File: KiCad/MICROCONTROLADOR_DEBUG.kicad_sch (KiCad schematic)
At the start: 9 parts, among them U7 PIC24HJ128GP504-I_PT, Y1 8MHz

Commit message: Errors solucionats
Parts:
- renumbered U7 to U1
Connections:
- net VDD_3V3 renamed +3.3V
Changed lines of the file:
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@@
-		)
-	)
-	(hierarchical_label "VDD_3V3"
-		(shape input)
-		(at 50.8 27.94 180)
-		(effects
-			(font
-				(size 1.27 1.27)
-			)
-			(justify right)
 		)
 	)
@@
 		(on_board yes)
 		(dnp no)
-		(property "Reference" "#FLG01"
+		(property "Reference" "#FLG02"
 			(at 78.74 48.895 0)
 			(effects
@@
 			(project ""
 				(path "/347831db-5db9-4aff-ad32-e56fd770e219/1f039355-d395-4709-b940-eff82ebe0f62"
-					(reference "#FLG01")
+					(reference "#FLG02")
 					(unit 1)
 				)
@@
 		(dnp no)
 		(fields_autoplaced yes)
-		(property "Reference" "U7"
+		(property "Reference" "U1"
 			(at 152.4 30.48 0)
 			(effects
@@
 			(project ""
 				(path "/347831db-5db9-4aff-ad32-e56fd770e219/1f039355-d395-4709-b940-eff82ebe0f62"
-					(reference "U7")
+					(reference "U1")
 					(unit 1)
 				)
@@
 		(dnp no)
 		(fields_autoplaced yes)
-		(property "Reference" "#PWR048"
+		(property "Reference" "#PWR09"
 			(at 68.58 59.69 0)
 			(effects
@@
 			(project "PROJECTE_EINES"
 				(path "/347831db-5db9-4aff-ad32-e56fd770e219/1f039355-d395-4709-b940-eff82ebe0f62"
-					(reference "#PWR048")
+					(reference "#PWR09")
 					(unit 1)
 				)
@@
 		(dnp no)
 		(fields_autoplaced yes)
-		(property "Reference" "#PWR09"
+		(property "Reference" "#PWR06"
 			(at 44.45 91.44 0)
 			(effects
@@
 			(project "PROJECTE_EINES"
 				(path "/347831db-5db9-4aff-ad32-e56fd770e219/1f039355-d395-4709-b940-eff82ebe0f62"
-					(reference "#PWR09")
+					(reference "#PWR06")
 					(unit 1)
 				)
@@
 		(dnp no)
 		(fields_autoplaced yes)
-		(property "Reference" "#PWR010"
+		(property "Reference" "#PWR07"
 			(at 60.96 91.44 0)
 			(effects
@@
 			(project "PROJECTE_EINES"
 				(path "/347831db-5db9-4aff-ad32-e56fd770e219/1f039355-d395-4709-b940-eff82ebe0f62"
-					(reference "#PWR010")
+					(reference "#PWR07")
+					(unit 1)
+				)
+			)
+		)
+	)
+	(symbol
+		(lib_id "power:+3.3V")
+		(at 50.8 27.94 0)
+		(unit 1)
+		(exclude_from_sim no)
+		(in_bom yes)
+		(on_board yes)
+		(dnp no)
+		(fields_autoplaced yes)
+		(property "Reference" "#PWR048"
+			(at 50.8 31.75 0)
+			(effects
+				(font
+					(size 1.27 1.27)
+				)
+				(hide yes)
+			)
+		)
+		(property "Value" "+3.3V"
+			(at 50.8 22.86 0)
+			(effects
+				(font
+					(size 1.27 1.27)
+				)
+			)
+		)
+		(property "Footprint" ""
+			(at 50.8 27.94 0)
+			(effects
+				(font
+					(size 1.27 1.27)
+				)
+				(hide yes)
+			)
+		)
+		(property "Datasheet" ""
+			(at 50.8 27.94 0)
+			(effects
+				(font
+					(size 1.27 1.27)
+				)
+				(hide yes)
+			)
+		)
+		(property "Description" "Power symbol creates a global label with name \"+3.3V\""
+			(at 50.8 27.94 0)
+			(effects
+				(font
+					(size 1.27 1.27)
+				)
+				(hide yes)
+			)
+		)
+		(pin "1"
+		)
+		(instances
+			(project ""
+				(path "/347831db-5db9-4aff-ad32-e56fd770e219/1f039355-d395-4709-b940-eff82ebe0f62"
+					(reference "#PWR048")
 					(unit 1)
 				)
@@
 		(dnp no)
 		(fields_autoplaced yes)
-		(property "Reference" "#PWR047"
+		(property "Reference" "#PWR08"
 			(at 67.31 44.45 0)
 			(effects
@@
 			(project "PROJECTE_EINES"
 				(path "/347831db-5db9-4aff-ad32-e56fd770e219/1f039355-d395-4709-b940-eff82ebe0f62"
-					(reference "#PWR047")
+					(reference "#PWR08")
 					(unit 1)
 				)
@@
 		(dnp no)
 		(fields_autoplaced yes)
-		(property "Reference" "#PWR045"
+		(property "Reference" "#PWR011"
 			(at 86.36 137.16 0)
 			(effects
@@
 			(project ""
 				(path "/347831db-5db9-4aff-ad32-e56fd770e219/1f039355-d395-4709-b940-eff82ebe0f62"
-					(reference "#PWR045")
+					(reference "#PWR011")
 					(unit 1)
 				)
@@
 		(dnp no)
 		(fields_autoplaced yes)
-		(property "Reference" "#PWR046"
+		(property "Reference" "#PWR010"
 			(at 78.74 58.42 0)
 			(effects
@@
 			(project "PROJECTE_EINES"
 				(path "/347831db-5db9-4aff-ad32-e56fd770e219/1f039355-d395-4709-b940-eff82ebe0f62"
-					(reference "#PWR046")
+					(reference "#PWR010")
 					(unit 1)
 				)
@@
 		(on_board yes)
 		(dnp no)
-		(property "Reference" "#FLG02"
+		(property "Reference" "#FLG03"
 			(at 93.98 48.895 0)
 			(effects
@@
 			(project "PROJECTE_EINES"
 				(path "/347831db-5db9-4aff-ad32-e56fd770e219/1f039355-d395-4709-b940-eff82ebe0f62"
-					(reference "#FLG02")
-					(unit 1)
-				)
+					(reference "#FLG03")
+					(unit 1)
+				)

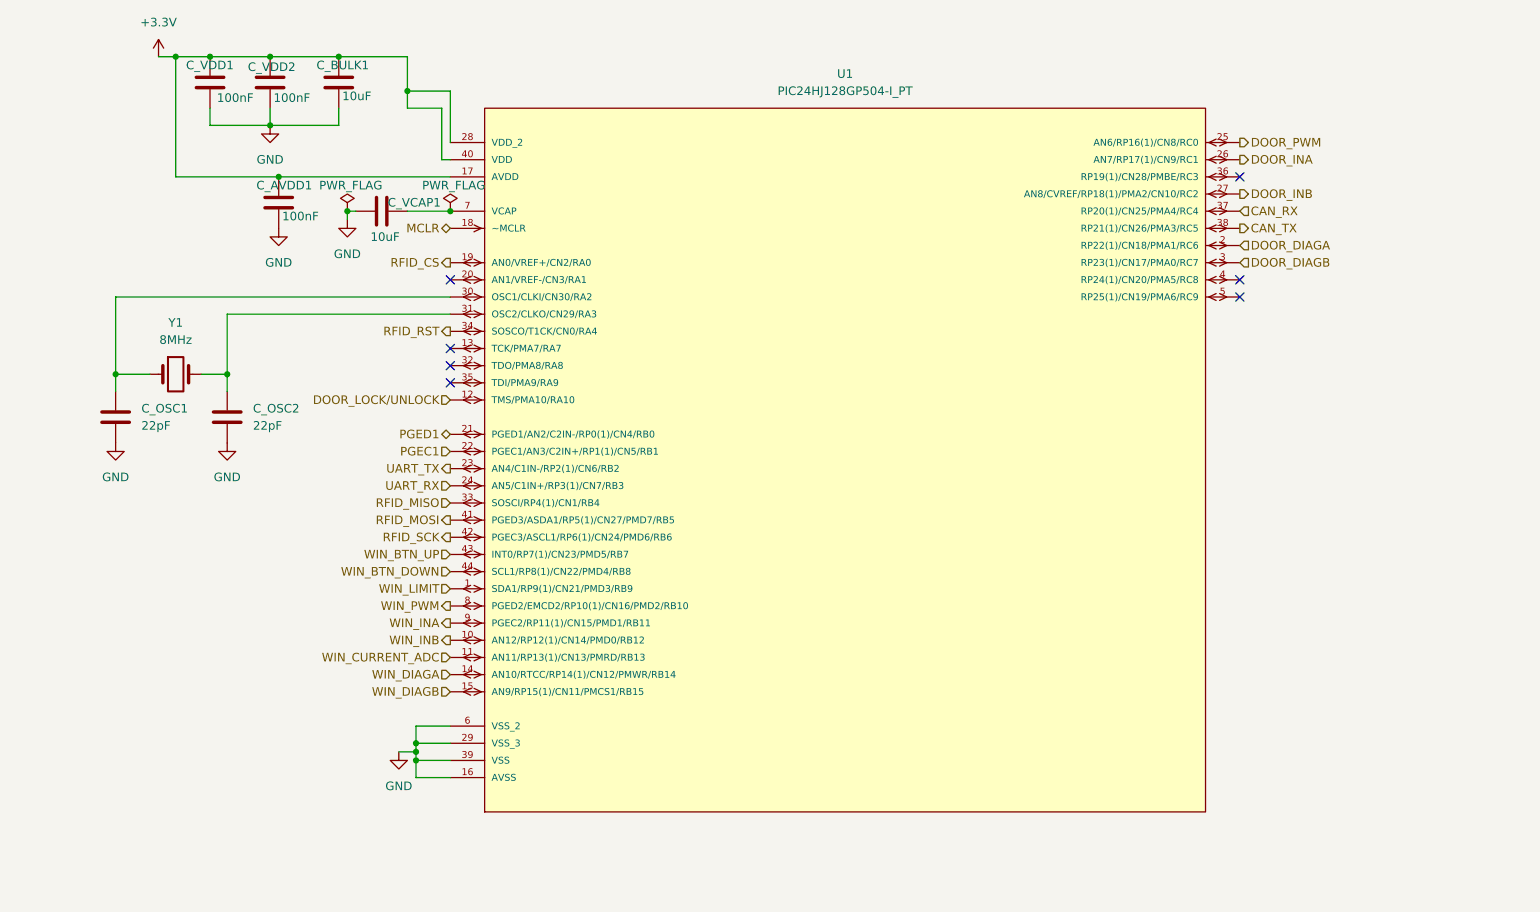
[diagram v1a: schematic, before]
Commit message: REORDENACIÓ DEL MICRO
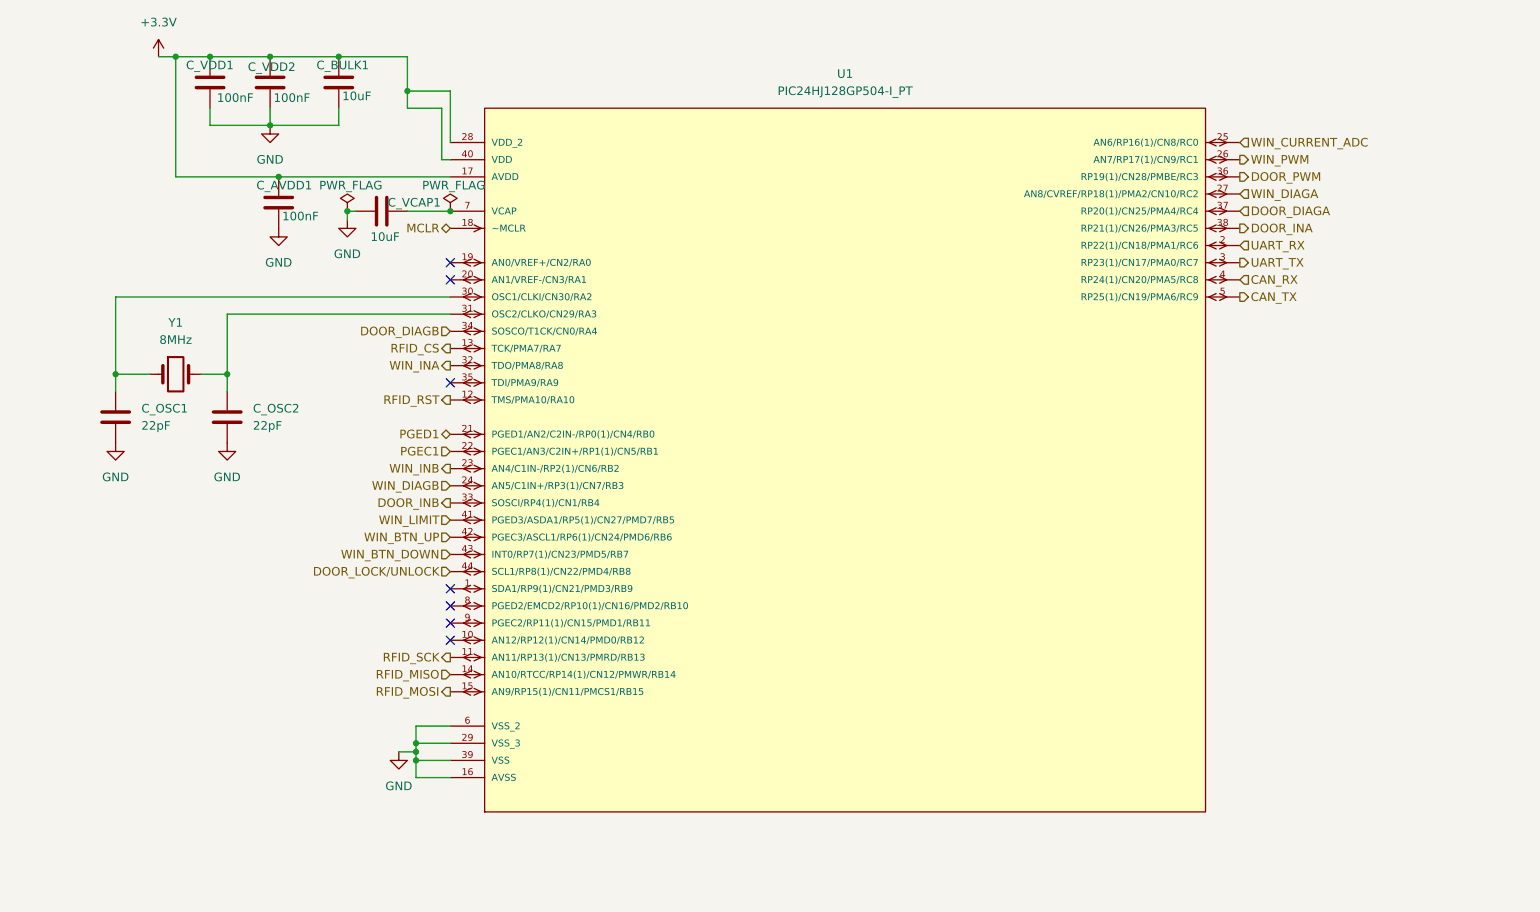
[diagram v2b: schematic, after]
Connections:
- net CAN_RX: now also U1.4 (RP24(1)/CN20/PMA5/RC8); no longer U1.37 (RP20(1)/CN25/PMA4/RC4)
- net CAN_TX: now also U1.5 (RP25(1)/CN19/PMA6/RC9); no longer U1.38 (RP21(1)/CN26/PMA3/RC5)
- net DOOR_DIAGA: now also U1.37 (RP20(1)/CN25/PMA4/RC4); no longer U1.2 (RP22(1)/CN18/PMA1/RC6)
- net DOOR_DIAGB: now also U1.34 (SOSCO/T1CK/CN0/RA4); no longer U1.3 (RP23(1)/CN17/PMA0/RC7)
- net DOOR_INA: now also U1.38 (RP21(1)/CN26/PMA3/RC5); no longer U1.26 (AN7/RP17(1)/CN9/RC1)
- net DOOR_INB: now also U1.33 (SOSCI/RP4(1)/CN1/RB4); no longer U1.27 (AN8/CVREF/RP18(1)/PMA2/CN10/RC2)
- net DOOR_LOCK/UNLOCK: now also U1.44 (SCL1/RP8(1)/CN22/PMD4/RB8); no longer U1.12 (TMS/PMA10/RA10)
- net DOOR_PWM: now also U1.36 (RP19(1)/CN28/PMBE/RC3); no longer U1.25 (AN6/RP16(1)/CN8/RC0)
- net RFID_CS: now also U1.13 (TCK/PMA7/RA7); no longer U1.19 (AN0/VREF+/CN2/RA0)
- net RFID_MISO: now also U1.14 (AN10/RTCC/RP14(1)/CN12/PMWR/RB14); no longer U1.33 (SOSCI/RP4(1)/CN1/RB4)
- net RFID_MOSI: now also U1.15 (AN9/RP15(1)/CN11/PMCS1/RB15); no longer U1.41 (PGED3/ASDA1/RP5(1)/CN27/PMD7/RB5)
- net RFID_RST: now also U1.12 (TMS/PMA10/RA10); no longer U1.34 (SOSCO/T1CK/CN0/RA4)
- net RFID_SCK: now also U1.11 (AN11/RP13(1)/CN13/PMRD/RB13); no longer U1.42 (PGEC3/ASCL1/RP6(1)/CN24/PMD6/RB6)
- net UART_RX: now also U1.2 (RP22(1)/CN18/PMA1/RC6); no longer U1.24 (AN5/C1IN+/RP3(1)/CN7/RB3)
- net UART_TX: now also U1.3 (RP23(1)/CN17/PMA0/RC7); no longer U1.23 (AN4/C1IN-/RP2(1)/CN6/RB2)
- net WIN_BTN_DOWN: now also U1.43 (INT0/RP7(1)/CN23/PMD5/RB7); no longer U1.44 (SCL1/RP8(1)/CN22/PMD4/RB8)
- net WIN_BTN_UP: now also U1.42 (PGEC3/ASCL1/RP6(1)/CN24/PMD6/RB6); no longer U1.43 (INT0/RP7(1)/CN23/PMD5/RB7)
- net WIN_CURRENT_ADC: now also U1.25 (AN6/RP16(1)/CN8/RC0); no longer U1.11 (AN11/RP13(1)/CN13/PMRD/RB13)
- net WIN_DIAGA: now also U1.27 (AN8/CVREF/RP18(1)/PMA2/CN10/RC2); no longer U1.14 (AN10/RTCC/RP14(1)/CN12/PMWR/RB14)
- net WIN_DIAGB: now also U1.24 (AN5/C1IN+/RP3(1)/CN7/RB3); no longer U1.15 (AN9/RP15(1)/CN11/PMCS1/RB15)
- net WIN_INA: now also U1.32 (TDO/PMA8/RA8); no longer U1.9 (PGEC2/RP11(1)/CN15/PMD1/RB11)
- net WIN_INB: now also U1.23 (AN4/C1IN-/RP2(1)/CN6/RB2); no longer U1.10 (AN12/RP12(1)/CN14/PMD0/RB12)
- net WIN_LIMIT: now also U1.41 (PGED3/ASDA1/RP5(1)/CN27/PMD7/RB5); no longer U1.1 (SDA1/RP9(1)/CN21/PMD3/RB9)
- net WIN_PWM: now also U1.26 (AN7/RP17(1)/CN9/RC1); no longer U1.8 (PGED2/EMCD2/RP10(1)/CN16/PMD2/RB10)
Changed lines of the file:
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@@
 	(paper "A4")
 	(junction
+		(at 58.42 27.94)
+		(diameter 0)
+		(color 0 0 0 0)
+	)
+	(junction
+		(at 68.58 45.72)
+		(diameter 0)
+		(color 0 0 0 0)
+	)
+	(junction
+		(at 60.96 74.93)
+		(diameter 0)
+		(color 0 0 0 0)
+	)
+	(junction
+		(at 53.34 27.94)
+		(diameter 0)
+		(color 0 0 0 0)
+	)
+	(junction
+		(at 77.47 27.94)
+		(diameter 0)
+		(color 0 0 0 0)
+	)
+	(junction
 		(at 93.98 50.8)
 		(diameter 0)
@@
 	)
 	(junction
-		(at 58.42 27.94)
-		(diameter 0)
-		(color 0 0 0 0)
-	)
-	(junction
-		(at 68.58 45.72)
-		(diameter 0)
-		(color 0 0 0 0)
-	)
-	(junction
-		(at 60.96 74.93)
-		(diameter 0)
-		(color 0 0 0 0)
-	)
-	(junction
-		(at 53.34 27.94)
-		(diameter 0)
-		(color 0 0 0 0)
-	)
-	(junction
-		(at 77.47 27.94)
-		(diameter 0)
-		(color 0 0 0 0)
-	)
-	(junction
 		(at 88.9 129.54)
 		(diameter 0)
@@
 	)
 	(no_connect
-		(at 93.98 71.12)
-	)
-	(no_connect
-		(at 210.82 63.5)
+		(at 93.98 111.76)
 	)
 	(no_connect
@@
 	)
 	(no_connect
-		(at 210.82 60.96)
+		(at 93.98 76.2)
 	)
 	(no_connect
-		(at 93.98 73.66)
+		(at 93.98 106.68)
 	)
 	(no_connect
-		(at 93.98 76.2)
+		(at 93.98 114.3)
 	)
 	(no_connect
-		(at 210.82 45.72)
+		(at 93.98 109.22)
+	)
+	(no_connect
+		(at 93.98 58.42)
 	)
 	(wire
@@
 	(hierarchical_label "DOOR_DIAGB"
 		(shape input)
-		(at 210.82 58.42 0)
-		(effects
-			(font
-				(size 1.27 1.27)
-			)
-			(justify left)
+		(at 93.98 68.58 180)
+		(effects
+			(font
+				(size 1.27 1.27)
+			)
+			(justify right)
 		)
 	)
 	(hierarchical_label "DOOR_INB"
 		(shape output)
-		(at 210.82 48.26 0)
-		(effects
-			(font
-				(size 1.27 1.27)
-			)
-			(justify left)
+		(at 93.98 93.98 180)
+		(effects
+			(font
+				(size 1.27 1.27)
+			)
+			(justify right)
 		)
 	)
 	(hierarchical_label "WIN_BTN_UP"
 		(shape input)
+		(at 93.98 99.06 180)
+		(effects
+			(font
+				(size 1.27 1.27)
+			)
+			(justify right)
+		)
+	)
+	(hierarchical_label "WIN_CURRENT_ADC"
+		(shape input)
+		(at 210.82 40.64 0)
+		(effects
+			(font
+				(size 1.27 1.27)
+			)
+			(justify left)
+		)
+	)
+	(hierarchical_label "CAN_RX"
+		(shape input)
+		(at 210.82 60.96 0)
+		(effects
+			(font
+				(size 1.27 1.27)
+			)
+			(justify left)
+		)
+	)
+	(hierarchical_label "WIN_DIAGB"
+		(shape input)
+		(at 93.98 91.44 180)
+		(effects
+			(font
+				(size 1.27 1.27)
+			)
+			(justify right)
+		)
+	)
+	(hierarchical_label "RFID_CS"
+		(shape output)
+		(at 93.98 71.12 180)
+		(effects
+			(font
+				(size 1.27 1.27)
+			)
+			(justify right)
+		)
+	)
+	(hierarchical_label "UART_RX"
+		(shape input)
+		(at 210.82 55.88 0)
+		(effects
+			(font
+				(size 1.27 1.27)
+			)
+			(justify left)
+		)
+	)
+	(hierarchical_label "RFID_MOSI"
+		(shape output)
+		(at 93.98 121.92 180)
+		(effects
+			(font
+				(size 1.27 1.27)
+			)
+			(justify right)
+		)
+	)
+	(hierarchical_label "WIN_BTN_DOWN"
+		(shape input)
 		(at 93.98 101.6 180)
 		(effects
@@
 		)
 	)
-	(hierarchical_label "WIN_CURRENT_ADC"
-		(shape input)
-		(at 93.98 116.84 180)
-		(effects
-			(font
-				(size 1.27 1.27)
-			)
-			(justify right)
-		)
-	)
-	(hierarchical_label "CAN_RX"
-		(shape input)
-		(at 210.82 50.8 0)
-		(effects
-			(font
-				(size 1.27 1.27)
-			)
-			(justify left)
-		)
-	)
-	(hierarchical_label "WIN_DIAGB"
-		(shape input)
-		(at 93.98 121.92 180)
-		(effects
-			(font
-				(size 1.27 1.27)
-			)
-			(justify right)
-		)
-	)
-	(hierarchical_label "RFID_CS"
-		(shape output)
-		(at 93.98 58.42 180)
-		(effects
-			(font
-				(size 1.27 1.27)
-			)
-			(justify right)
-		)
-	)
-	(hierarchical_label "UART_RX"
-		(shape input)
-		(at 93.98 91.44 180)
-		(effects
-			(font
-				(size 1.27 1.27)
-			)
-			(justify right)
-		)
-	)
-	(hierarchical_label "RFID_MOSI"
-		(shape output)
-		(at 93.98 96.52 180)
-		(effects
-			(font
-				(size 1.27 1.27)
-			)
-			(justify right)
-		)
-	)
-	(hierarchical_label "WIN_BTN_DOWN"
-		(shape input)
-		(at 93.98 104.14 180)
-		(effects
-			(font
-				(size 1.27 1.27)
-			)
-			(justify right)
-		)
-	)
 	(hierarchical_label "CAN_TX"
 		(shape output)
-		(at 210.82 53.34 0)
+		(at 210.82 63.5 0)
 		(effects
 			(font
@@
 	(hierarchical_label "WIN_PWM"
 		(shape output)
-		(at 93.98 109.22 180)
-		(effects
-			(font
-				(size 1.27 1.27)
-			)
-			(justify right)
+		(at 210.82 43.18 0)
+		(effects
+			(font
+				(size 1.27 1.27)
+			)
+			(justify left)
 		)
 	)
 	(hierarchical_label "RFID_SCK"
 		(shape output)
-		(at 93.98 99.06 180)
+		(at 93.98 116.84 180)
 		(effects
 			(font
@@
 	(hierarchical_label "RFID_RST"
 		(shape output)
-		(at 93.98 68.58 180)
+		(at 93.98 78.74 180)
 		(effects
 			(font
@@
 	(hierarchical_label "DOOR_INA"
 		(shape output)
-		(at 210.82 43.18 0)
+		(at 210.82 53.34 0)
 		(effects
 			(font
@@
 	(hierarchical_label "RFID_MISO"
 		(shape input)
-		(at 93.98 93.98 180)
+		(at 93.98 119.38 180)
 		(effects
 			(font
@@
 	(hierarchical_label "DOOR_LOCK{slash}UNLOCK"
 		(shape input)
-		(at 93.98 78.74 180)
+		(at 93.98 104.14 180)
 		(effects
 			(font
@@
 	(hierarchical_label "WIN_DIAGA"
 		(shape input)
-		(at 93.98 119.38 180)
-		(effects
-			(font
-				(size 1.27 1.27)
-			)
-			(justify right)
+		(at 210.82 48.26 0)
+		(effects
+			(font
+				(size 1.27 1.27)
+			)
+			(justify left)
 		)
 	)
 	(hierarchical_label "WIN_INB"
 		(shape output)
-		(at 93.98 114.3 180)
+		(at 93.98 88.9 180)
 		(effects
 			(font
@@
 	(hierarchical_label "WIN_INA"
 		(shape output)
-		(at 93.98 111.76 180)
+		(at 93.98 73.66 180)
 		(effects
 			(font
@@
 	(hierarchical_label "DOOR_DIAGA"
 		(shape input)
-		(at 210.82 55.88 0)
+		(at 210.82 50.8 0)
 		(effects
 			(font
@@
 	(hierarchical_label "DOOR_PWM"
 		(shape output)
-		(at 210.82 40.64 0)
+		(at 210.82 45.72 0)
 		(effects
 			(font
@@
 	(hierarchical_label "WIN_LIMIT"
 		(shape input)
-		(at 93.98 106.68 180)
+		(at 93.98 96.52 180)
 		(effects
 			(font
@@
 	(hierarchical_label "UART_TX"
 		(shape output)
-		(at 93.98 88.9 180)
-		(effects
-			(font
-				(size 1.27 1.27)
-			)
-			(justify right)
-		)
-	)
+		(at 210.82 58.42 0)
+		(effects
+			(font
+				(size 1.27 1.27)
+			)
+			(justify left)
+		)
+	)

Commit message: V1 Routing
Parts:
- removed C_VDD1: 100nF, Capacitor_SMD:C_0603_1608Metric, symbol Device:C
- C_AVDD1, C_VDD2: footprint Capacitor_SMD:C_0603_1608Metric -> Capacitor_SMD:C_0805_2012Metric
- C_VCAP1: footprint Capacitor_SMD:C_1206_3216Metric -> Capacitor_SMD:C_0805_2012Metric
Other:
- moved on the sheet: C_BULK1, C_OSC2, U1, Y1
